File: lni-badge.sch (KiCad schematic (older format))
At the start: 4 parts

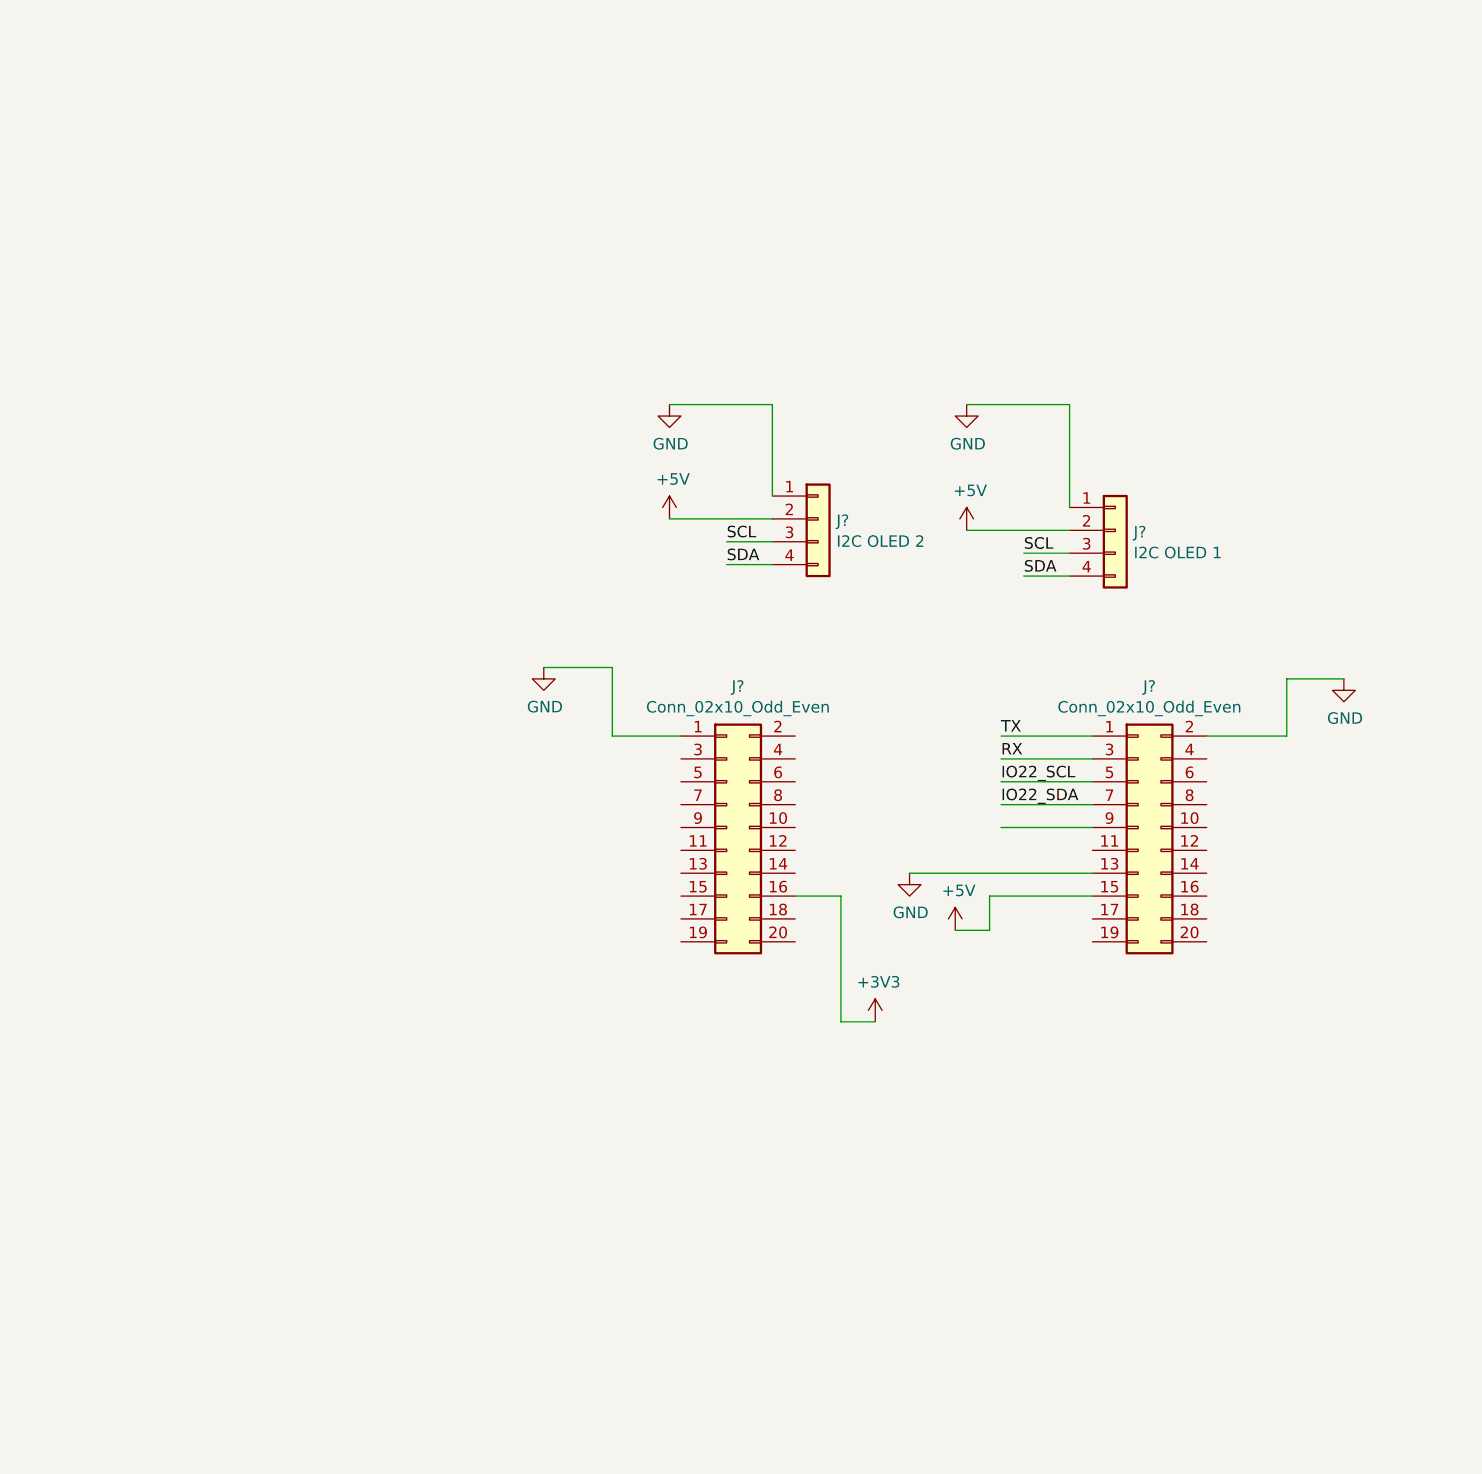
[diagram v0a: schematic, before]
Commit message: Added display connectors, clean up
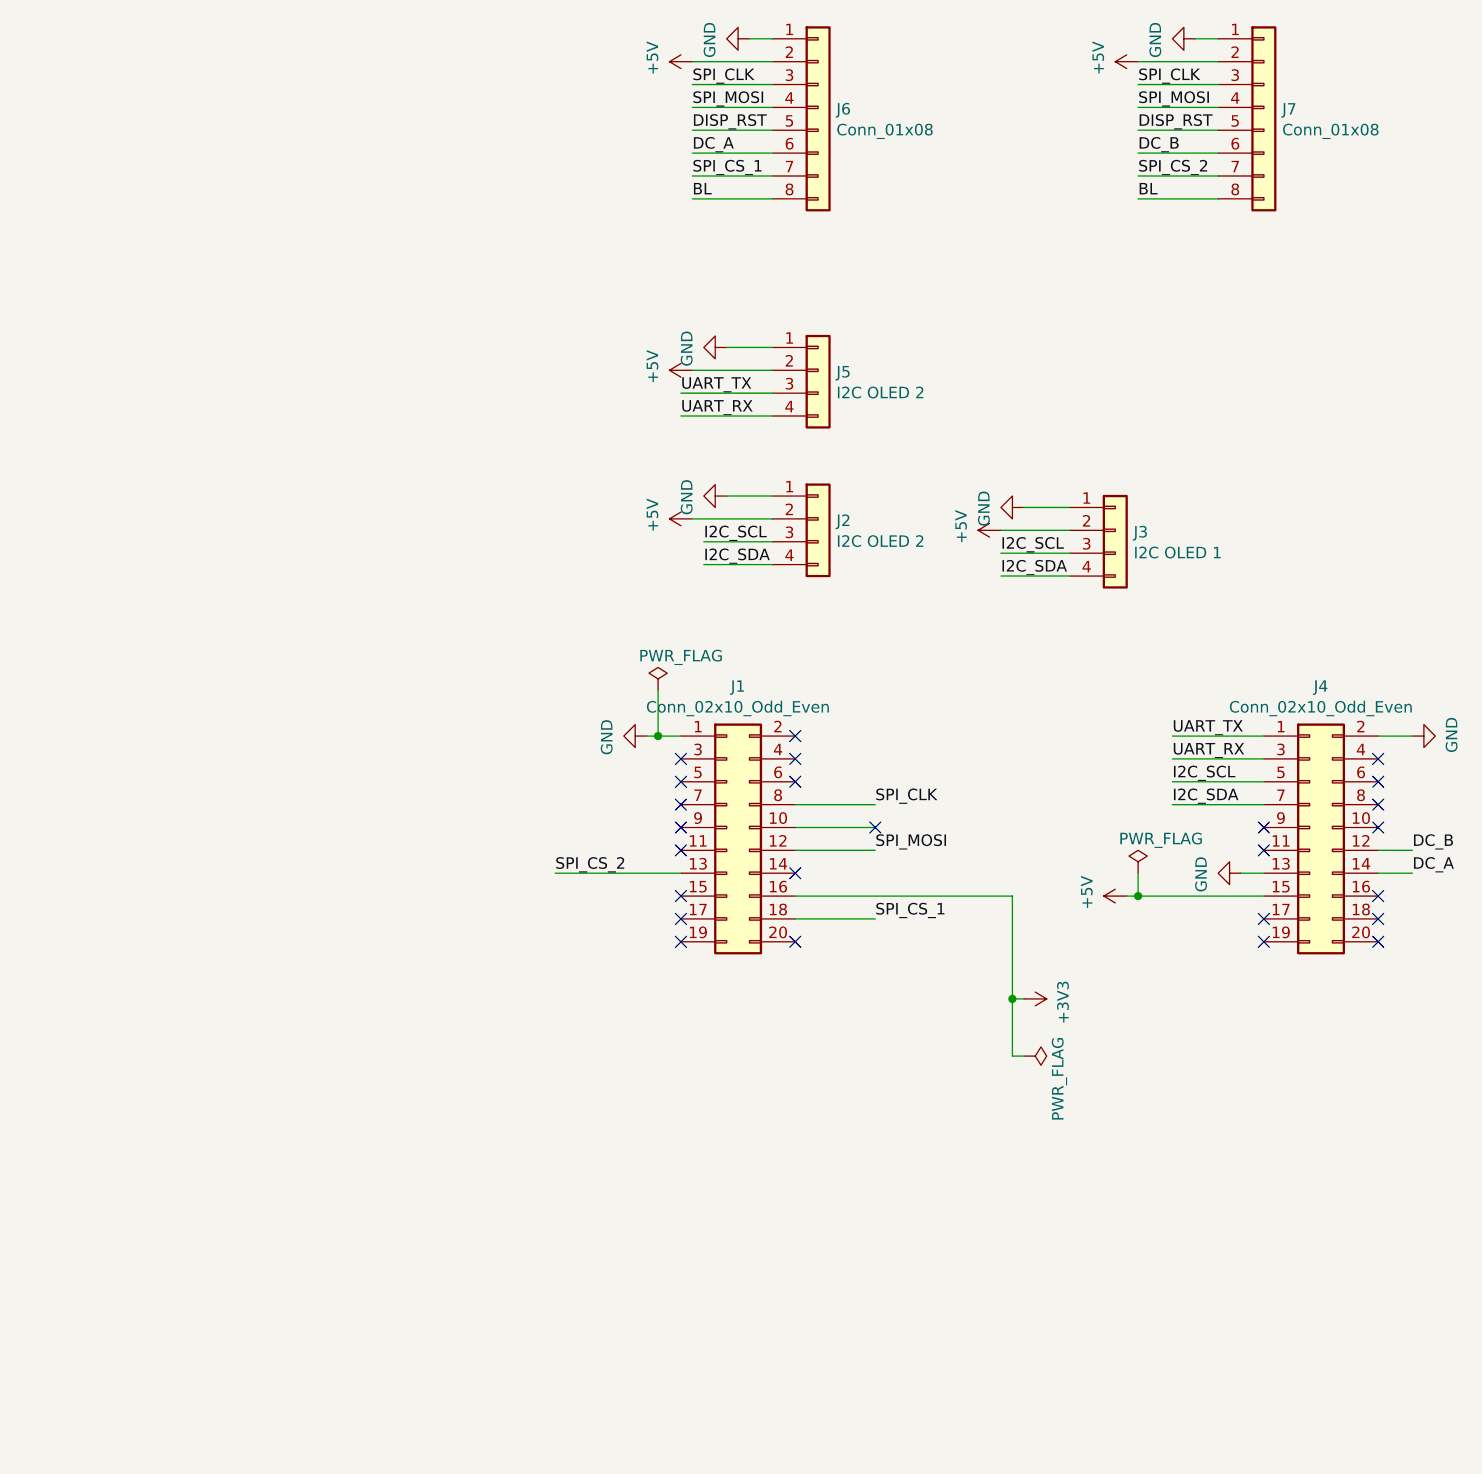
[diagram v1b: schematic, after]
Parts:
- added J5: I2C OLED 2, symbol Connector_Generic:Conn_01x04
- added J6, J7: Conn_01x08, symbol Connector_Generic:Conn_01x08
- gave numbers to parts that had none: 4
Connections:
- net labels added: BL, DC_A, DC_B, DISP_RST, I2C_SCL, I2C_SDA, SPI_CLK, SPI_CS_1, SPI_CS_2, SPI_MOSI, UART_RX, UART_TX
- net labels removed: IO22_SCL, IO22_SDA, RX, SCL, SDA, TX
- wire segments 28 -> 52
- no-connect marks 0 -> 25
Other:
- moved on the sheet: J4

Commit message: Added mechanics
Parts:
- added D1: LED, LED_THT:LED_D5.0mm, symbol Device:LED
- added H1, H2, H3, H4: MountingHole, MountingHole:MountingHole_5.3mm_M5_DIN965_Pad, symbol Mechanical:MountingHole
- added R1: R, Resistor_SMD:R_0603_1608Metric_Pad0.98x0.95mm_HandSolder, symbol Device:R
- J1, J4: footprint (none) -> Connector_PinHeader_2.54mm:PinHeader_2x10_P2.54mm_Vertical
- J2, J3, J5: footprint (none) -> Connector_PinHeader_2.54mm:PinHeader_1x04_P2.54mm_Vertical
- J6, J7: footprint (none) -> Connector_PinHeader_2.54mm:PinHeader_1x08_P2.54mm_Vertical
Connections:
- net GND: now also R1.2
- net at J1.7 (Pin_7): now also D1.2 (A)
- new net: D1.1 (K), R1.1
- no-connect marks 25 -> 24
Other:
- note added: "Mech"
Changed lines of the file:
@@
 F 0 "J3" H 5780 3542 50  0000 L CNN
 F 1 "I2C OLED 1" H 5780 3451 50  0000 L CNN
-F 2 "" H 5700 3550 50  0001 C CNN
+F 2 "Connector_PinHeader_2.54mm:PinHeader_1x04_P2.54mm_Vertical" H 5700 3550 50  0001 C CNN
 F 3 "~" H 5700 3550 50  0001 C CNN
 	1    5700 3550
@@
 F 0 "J2" H 4480 3492 50  0000 L CNN
 F 1 "I2C OLED 2" H 4480 3401 50  0000 L CNN
-F 2 "" H 4400 3500 50  0001 C CNN
+F 2 "Connector_PinHeader_2.54mm:PinHeader_1x04_P2.54mm_Vertical" H 4400 3500 50  0001 C CNN
 F 3 "~" H 4400 3500 50  0001 C CNN
 	1    4400 3500
@@
 F 0 "J1" H 4050 5467 50  0000 C CNN
 F 1 "Conn_02x10_Odd_Even" H 4050 5376 50  0000 C CNN
-F 2 "" H 4000 4850 50  0001 C CNN
+F 2 "Connector_PinHeader_2.54mm:PinHeader_2x10_P2.54mm_Vertical" H 4000 4850 50  0001 C CNN
 F 3 "~" H 4000 4850 50  0001 C CNN
 	1    4000 4850
@@
 F 0 "J4" H 6600 5467 50  0000 C CNN
 F 1 "Conn_02x10_Odd_Even" H 6600 5376 50  0000 C CNN
-F 2 "" H 6550 4850 50  0001 C CNN
+F 2 "Connector_PinHeader_2.54mm:PinHeader_2x10_P2.54mm_Vertical" H 6550 4850 50  0001 C CNN
 F 3 "~" H 6550 4850 50  0001 C CNN
 	1    6550 4850
@@
 NoConn ~ 3800 4950
 NoConn ~ 3800 4850
-NoConn ~ 3800 4750
 NoConn ~ 3800 4650
 NoConn ~ 3800 4550
@@
 F 0 "J5" H 4480 2842 50  0000 L CNN
 F 1 "I2C OLED 2" H 4480 2751 50  0000 L CNN
-F 2 "" H 4400 2850 50  0001 C CNN
+F 2 "Connector_PinHeader_2.54mm:PinHeader_1x04_P2.54mm_Vertical" H 4400 2850 50  0001 C CNN
 F 3 "~" H 4400 2850 50  0001 C CNN
 	1    4400 2850
@@
 F 0 "J6" H 4480 1692 50  0000 L CNN
 F 1 "Conn_01x08" H 4480 1601 50  0000 L CNN
-F 2 "" H 4400 1700 50  0001 C CNN
+F 2 "Connector_PinHeader_2.54mm:PinHeader_1x08_P2.54mm_Vertical" H 4400 1700 50  0001 C CNN
 F 3 "~" H 4400 1700 50  0001 C CNN
 	1    4400 1700
@@
 F 0 "J7" H 6430 1692 50  0000 L CNN
 F 1 "Conn_01x08" H 6430 1601 50  0000 L CNN
-F 2 "" H 6350 1700 50  0001 C CNN
+F 2 "Connector_PinHeader_2.54mm:PinHeader_1x08_P2.54mm_Vertical" H 6350 1700 50  0001 C CNN
 F 3 "~" H 6350 1700 50  0001 C CNN
 	1    6350 1700
@@
 Wire Wire Line
 	7000 5050 6850 5050
+$Comp
+L Device:LED D1
+U 1 1 6076164F
+P 2450 5000
+F 0 "D1" V 2489 4882 50  0000 R CNN
+F 1 "LED" V 2398 4882 50  0000 R CNN
+F 2 "LED_THT:LED_D5.0mm" H 2450 5000 50  0001 C CNN
+F 3 "~" H 2450 5000 50  0001 C CNN
+F 4 "0.10" V 2450 5000 50  0001 C CNN "Preis"
+	1    2450 5000
+	0    -1   -1   0
+$EndComp
+$Comp
+L Device:R R1
+U 1 1 607637E0
+P 2450 5450
+F 0 "R1" H 2520 5496 50  0000 L CNN
+F 1 "R" H 2520 5405 50  0000 L CNN
+F 2 "Resistor_SMD:R_0603_1608Metric_Pad0.98x0.95mm_HandSolder" V 2380 5450 50  0001 C CNN
+F 3 "~" H 2450 5450 50  0001 C CNN
+	1    2450 5450
+	1    0    0    -1
+$EndComp
+$Comp
+L power:GND #PWR07
+U 1 1 6076EC24
+P 2450 5750
+F 0 "#PWR07" H 2450 5500 50  0001 C CNN
+F 1 "GND" H 2455 5577 50  0000 C CNN
+F 2 "" H 2450 5750 50  0001 C CNN
+F 3 "" H 2450 5750 50  0001 C CNN
+	1    2450 5750
+	1    0    0    -1
+$EndComp
+Wire Wire Line
+	2450 5750 2450 5600
+Wire Wire Line
+	2450 4850 2450 4750
+Wire Wire Line
+	2450 4750 3800 4750
+Wire Wire Line
+	2450 5300 2450 5150
+$Comp
+L Mechanical:MountingHole H1
+U 1 1 609F3BAA
+P 1100 6600
+F 0 "H1" H 1200 6646 50  0000 L CNN
+F 1 "MountingHole" H 1200 6555 50  0000 L CNN
+F 2 "MountingHole:MountingHole_5.3mm_M5_DIN965_Pad" H 1100 6600 50  0001 C CNN
+F 3 "~" H 1100 6600 50  0001 C CNN
+	1    1100 6600
+	1    0    0    -1
+$EndComp
+Wire Notes Line
+	900  6350 4000 6350
+Wire Notes Line
+	4000 6350 4000 7600
+Wire Notes Line
+	4000 7600 900  7600
+Wire Notes Line
+	900  7600 900  6350
+Text Notes 950  6450 0    50   ~ 0
+Mech
+$Comp
+L Mechanical:MountingHole H2
+U 1 1 609F9441
+P 1100 6850
+F 0 "H2" H 1200 6896 50  0000 L CNN
+F 1 "MountingHole" H 1200 6805 50  0000 L CNN
+F 2 "MountingHole:MountingHole_5.3mm_M5_DIN965_Pad" H 1100 6850 50  0001 C CNN
+F 3 "~" H 1100 6850 50  0001 C CNN
+	1    1100 6850
+	1    0    0    -1
+$EndComp
+$Comp
+L Mechanical:MountingHole H3
+U 1 1 609F9647
+P 1100 7100
+F 0 "H3" H 1200 7146 50  0000 L CNN
+F 1 "MountingHole" H 1200 7055 50  0000 L CNN
+F 2 "MountingHole:MountingHole_5.3mm_M5_DIN965_Pad" H 1100 7100 50  0001 C CNN
+F 3 "~" H 1100 7100 50  0001 C CNN
+	1    1100 7100
+	1    0    0    -1
+$EndComp
+$Comp
+L Mechanical:MountingHole H4
+U 1 1 609F9915
+P 1100 7350
+F 0 "H4" H 1200 7396 50  0000 L CNN
+F 1 "MountingHole" H 1200 7305 50  0000 L CNN
+F 2 "MountingHole:MountingHole_5.3mm_M5_DIN965_Pad" H 1100 7350 50  0001 C CNN
+F 3 "~" H 1100 7350 50  0001 C CNN
+	1    1100 7350
+	1    0    0    -1
+$EndComp
 $EndSCHEMATC
